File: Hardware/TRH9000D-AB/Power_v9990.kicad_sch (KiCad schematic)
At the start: 47 parts, among them U1 V9990, U10 THS7374-lrj, U2 KM428C256, U3 KM428C256, U4 74VHC138, U5 T.I_SN74LVC2G32DCTR, U6 LMH1980, U7 AD8188, U8 LMH1980, U9 SST39SF010A-lrj

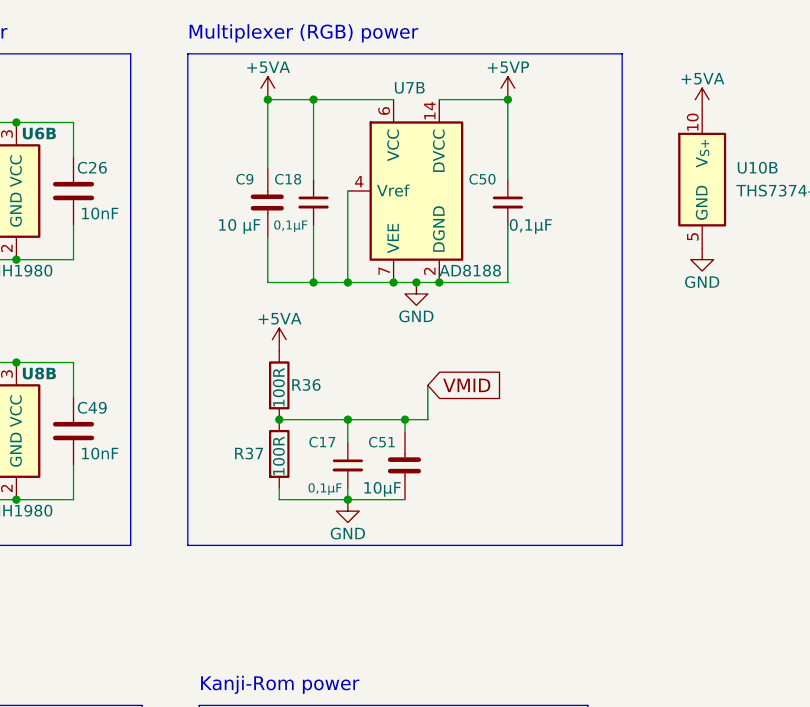
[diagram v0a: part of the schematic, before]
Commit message: Finished rerouting the AA-variant, and replaced the fuses with SMD-ones.
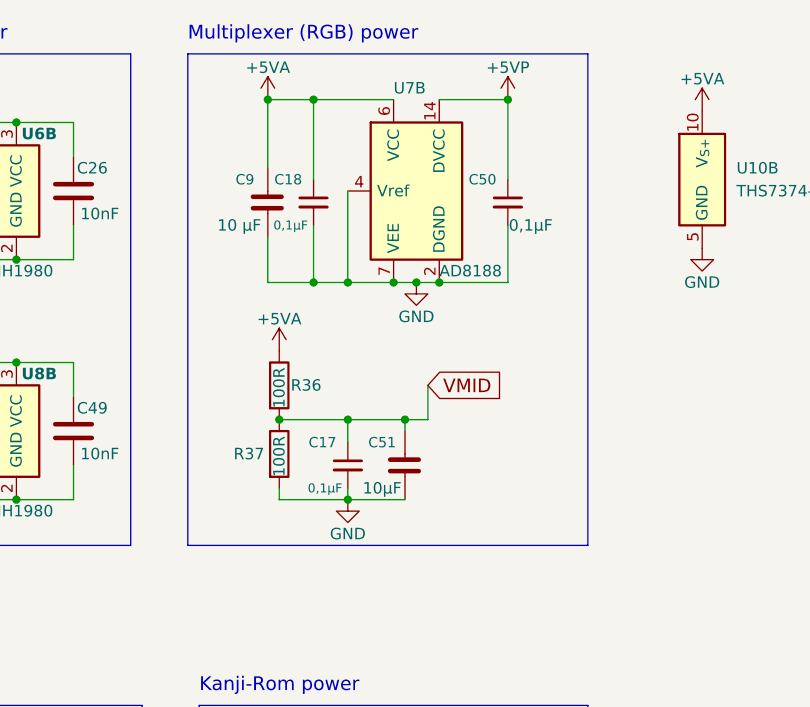
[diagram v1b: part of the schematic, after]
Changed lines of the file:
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@@
     (comment 2 "Shared under CERN-OHL-S license")
     (comment 3 "TRH9000 - Open Source MSX Graphics Card based on the Yamaha V9990")
-    (comment 4 "Designed  by: Cristiano Goncalves, Doomn00b, SD_Snatcher")
+    (comment 4 "Designed  by: Cristiano Goncalves, Doomn00b, SD_Snatcher & Sunrise")
   )
   (junction (at 285.75 30.48) (diameter 0) (color 0 0 0 0)
@@
     (stroke (width 0) (type default) (color 0 0 0 0))
   )
-  (polyline (pts (xy 325.12 25.4) (xy 325.12 80.01))
+  (polyline (pts (xy 321.31 25.4) (xy 321.31 80.01))
     (stroke (width 0) (type default) (color 0 0 0 0))
   )
@@
     (stroke (width 0) (type default) (color 0 0 0 0))
   )
-  (polyline (pts (xy 325.12 80.01) (xy 276.86 80.01))
+  (polyline (pts (xy 321.31 80.01) (xy 276.86 80.01))
     (stroke (width 0) (type default) (color 0 0 0 0))
   )
@@
     (stroke (width 0) (type default) (color 0 0 0 0))
   )
-  (polyline (pts (xy 276.86 25.4) (xy 325.12 25.4))
-    (stroke (width 0) (type default) (color 0 0 0 0))
-  )
+  (polyline (pts (xy 276.86 25.4) (xy 321.31 25.4))
+    (stroke (width 0) (type default) (color 0 0 0 0))
+  )
